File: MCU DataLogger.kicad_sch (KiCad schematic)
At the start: 0 parts

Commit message: Have added required symbols
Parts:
- added BT?: Battery, symbol Device:Battery
- added C? (x4): C, symbol Device:C
- added C? (x2): C_Polarized, symbol Device:C_Polarized
- added D? (x2): LED, symbol Device:LED
- added H? (x4): MountingHole, symbol Mechanical:MountingHole
- added R? (x7): R, symbol Device:R
- added U?: DS1337S+, SOIC127P600X175-8N, symbol DS1337S_:DS1337S+
- added U? (x2): 24LC1025, symbol Memory_EEPROM:24LC1025
- added U?: ATMEGA328P-AU, QFP80P900X900X120-32N, symbol ATMEGA328P-AU:ATMEGA328P-AU
- added Y? (x2): Crystal, symbol Device:Crystal
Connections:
- new net: U?.21 (GND), U?.3 (GND), U?.5 (GND)
- new net: U?.4 (VCC), U?.6 (VCC)
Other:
- added sheet Connectors (connectors.kicad_sch)

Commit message: Changes and add component values
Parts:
- removed C?: C_Polarized, symbol Device:C_Polarized
- C1, C4: renamed from C?; value C -> 0.1uF
- C2, C3: renamed from C?; value C -> 22pF
- C5: renamed from C?; value C_Polarized -> 100nF
- R1, R2: renamed from R?; value R -> 4.7K
- R3, R4, R6: renamed from R?; value R -> 10K
- R5, R7: renamed from R?; value R -> 330
- Y1: renamed from Y?; value Crystal -> 32.768 KHz
- Y2: renamed from Y?; value Crystal -> 16 MHz
- gave numbers to parts that had none: 11
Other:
- moved on the sheet: BT1, C1, C2, C3, C4, C5, D1, D2, R1, R2, R3, R4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

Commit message: Completed symbol-footprint associations.
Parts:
- BT1: footprint (none) -> Connector_PinHeader_2.54mm:PinHeader_1x02_P2.54mm_Vertical
- C1, C2, C3, C4, C5: footprint (none) -> Capacitor_SMD:C_0805_2012Metric
- D1, D2: footprint (none) -> LED_SMD:LED_0805_2012Metric
- H1, H2, H3, H4: footprint (none) -> MountingHole:MountingHole_2.1mm
- R1, R2, R3, R4, R5, R6, R7: footprint (none) -> Resistor_SMD:R_0805_2012Metric
- U1, U2: footprint (none) -> Package_SO:SOIC-8_5.23x5.23mm_P1.27mm
- U3: footprint SOIC127P600X175-8N -> Libraries:SOIC127P600X175-8N
- U4: footprint QFP80P900X900X120-32N -> Libraries:QFP80P900X900X120-32N
- Y1, Y2: footprint (none) -> Crystal:Crystal_SMD_5032-2Pin_5.0x3.2mm_HandSoldering

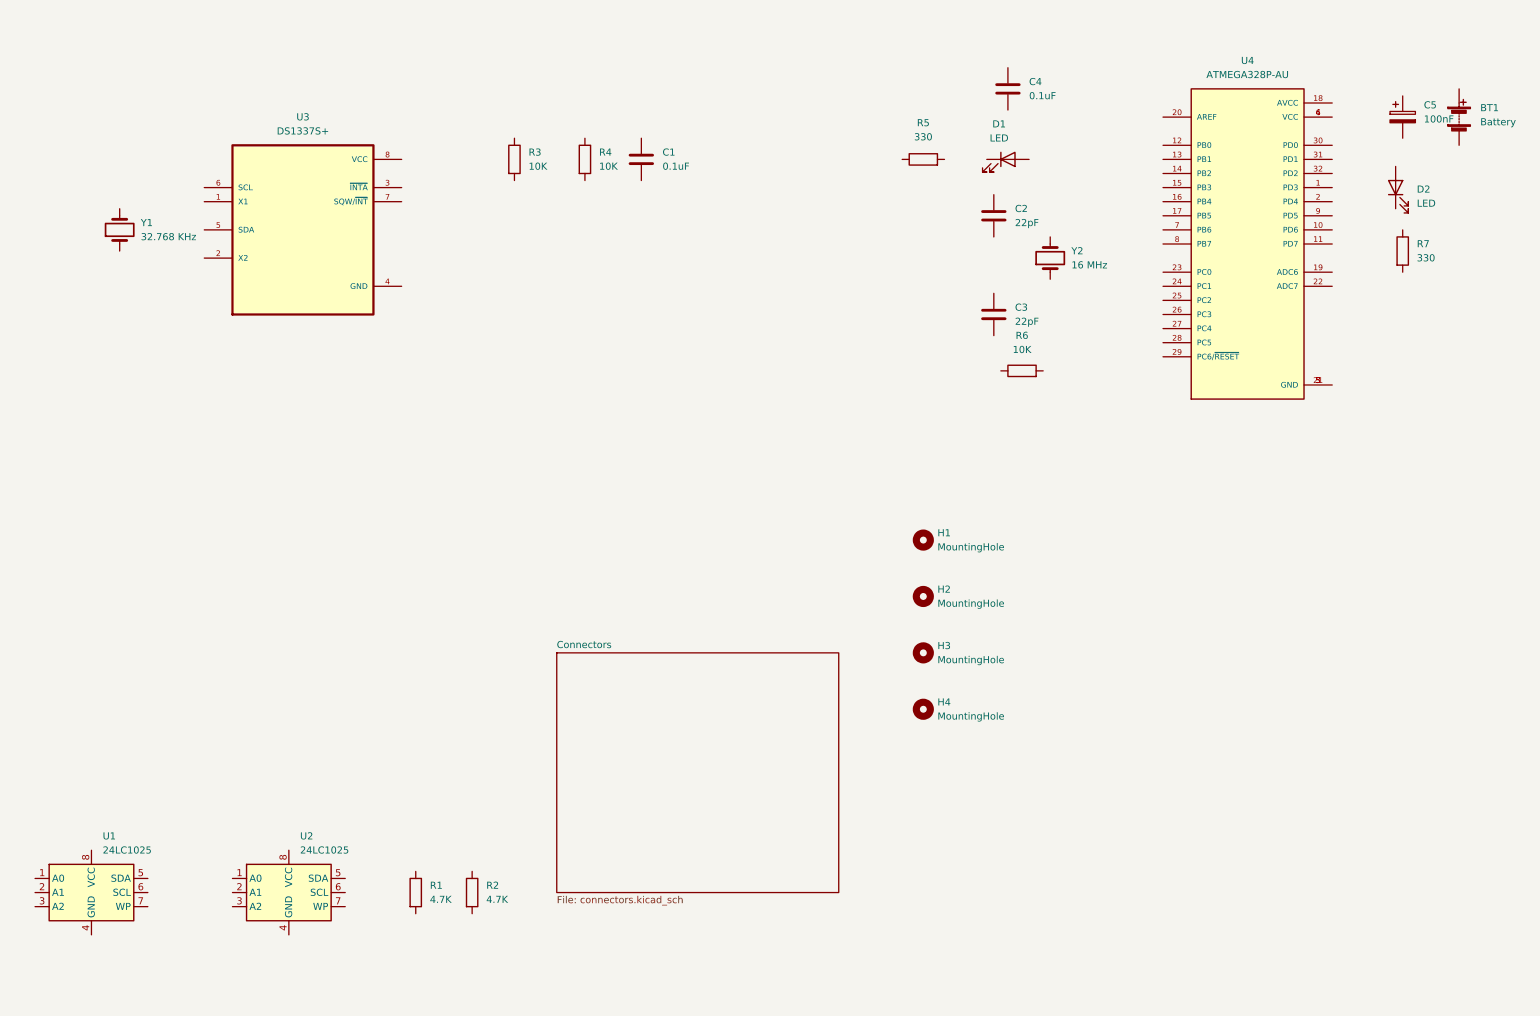
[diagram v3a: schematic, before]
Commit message: Completed wiring of main sheet.
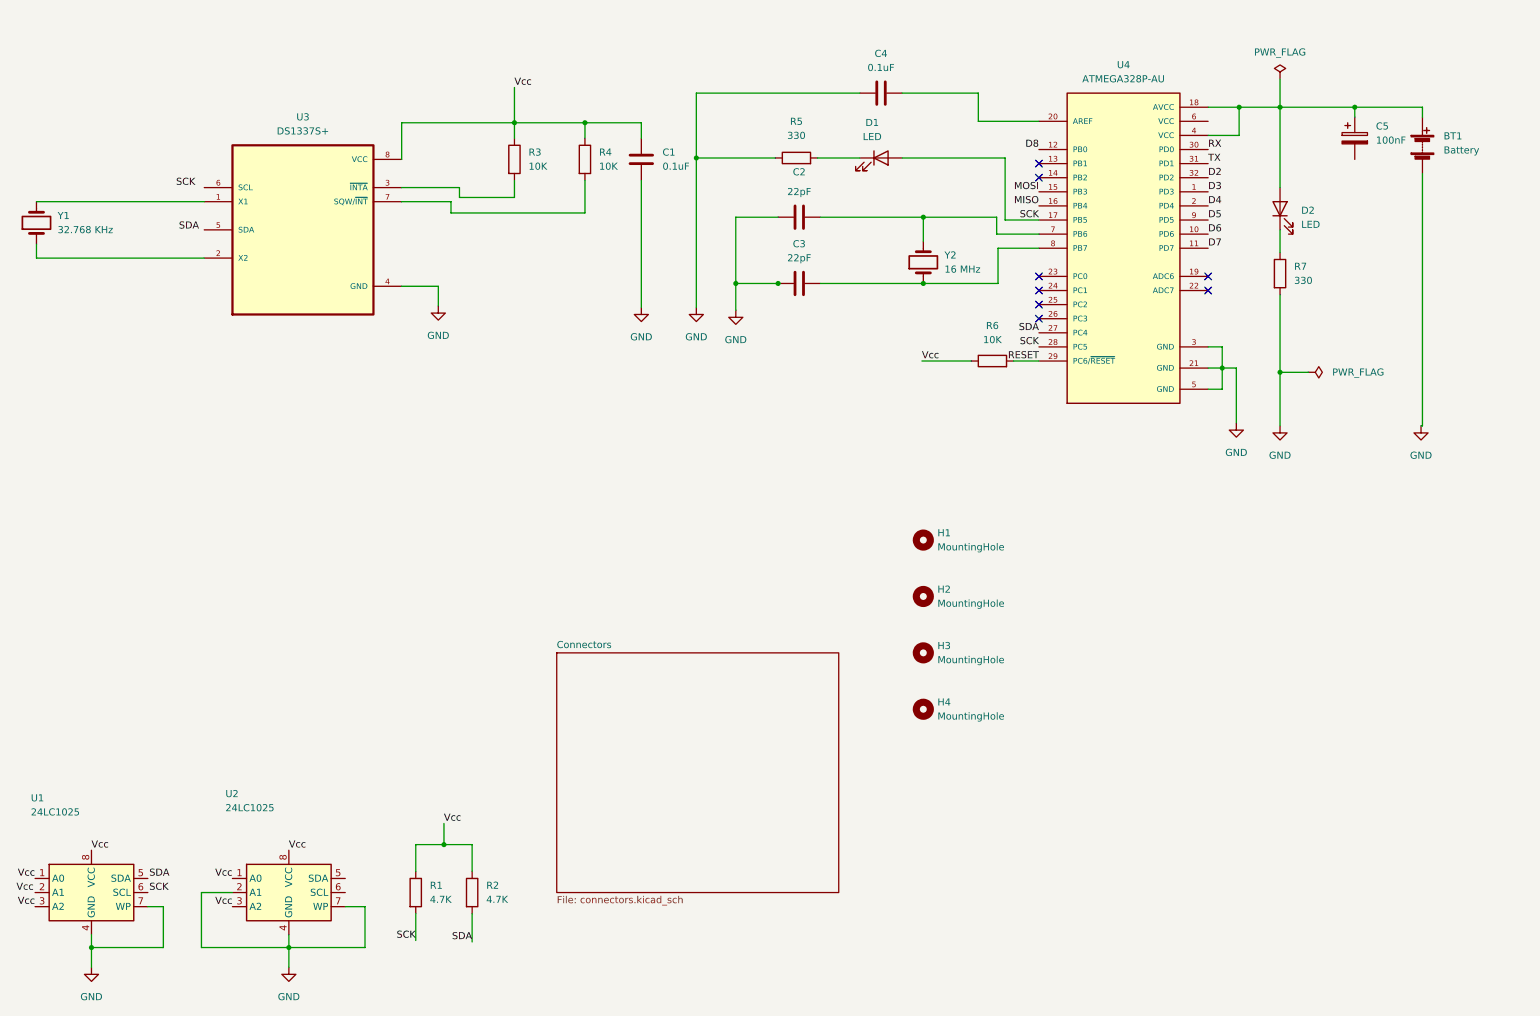
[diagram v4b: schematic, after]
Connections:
- net Vcc: now reaches R6.1
- net Vcc: now also R1.1, R2.1, U1.1 (A0), U1.3 (A2), U1.8 (VCC), U2.1 (A0), U2.3 (A2), U2.8 (VCC)
- net RESET: now reaches R6.2
- net RESET: now also U4.29 (PC6/~{RESET})
- net at U3.1 (X1): now also Y1.2
- net at U3.2 (X2): now also Y1.1
- net at U3.3 (~{INTA}): now also R3.2
- net GND: now reaches U3.4 (GND)
- net GND: now also BT1.2 (-), C1.2, C2.2, C3.1, C4.1, R5.1, R7.2, U1.4 (GND), U1.7 (WP), U2.2 (A1), U2.4 (GND), U2.7 (WP), U4.21 (GND), U4.3 (GND), U4.5 (GND)
- net at U3.7 (SQW/~{INT}): now also R4.2
- net at U3.8 (VCC): now also C1.1, R3.1, R4.1
- net at R7.1: now also D2.1 (K)
- net at C2.1: now also U4.7 (PB6), Y2.2
- net D3: now reaches U4.1 (PD3)
- net D6: now reaches U4.10 (PD6)
- net D7: now reaches U4.11 (PD7)
- net D8: now reaches U4.12 (PB0)
- net MOSI: now reaches U4.15 (PB3)
- net MISO: now reaches U4.16 (PB4)
- net SCK: now reaches U4.17 (PB5)
- net SCK: now also D1.2 (A), R1.2, U4.28 (PC5)
- net at U4.18 (AVCC): now also BT1.1 (+), C5.1, D2.2 (A), U4.4 (VCC)
- net D4: now reaches U4.2 (PD4)
- net at U4.20 (AREF): now also C4.2
- net SDA: now reaches U4.27 (PC4)
- net SDA: now also R2.2
- net RX: now reaches U4.30 (PD0)
- net TX: now reaches U4.31 (PD1)
- net D2: now reaches U4.32 (PD2)
- net at U4.6 (VCC): no longer U4.4 (VCC)
- net at U4.8 (PB7): now also C3.2, Y2.1
- net D5: now reaches U4.9 (PD5)
- net at R5.2: now also D1.1 (K)
- no-connect marks 0 -> 8
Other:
- moved on the sheet: BT1, C2, C3, C4, C5, D1, D2, R5, R6, R7, Y1, Y2

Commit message: Completed wiring
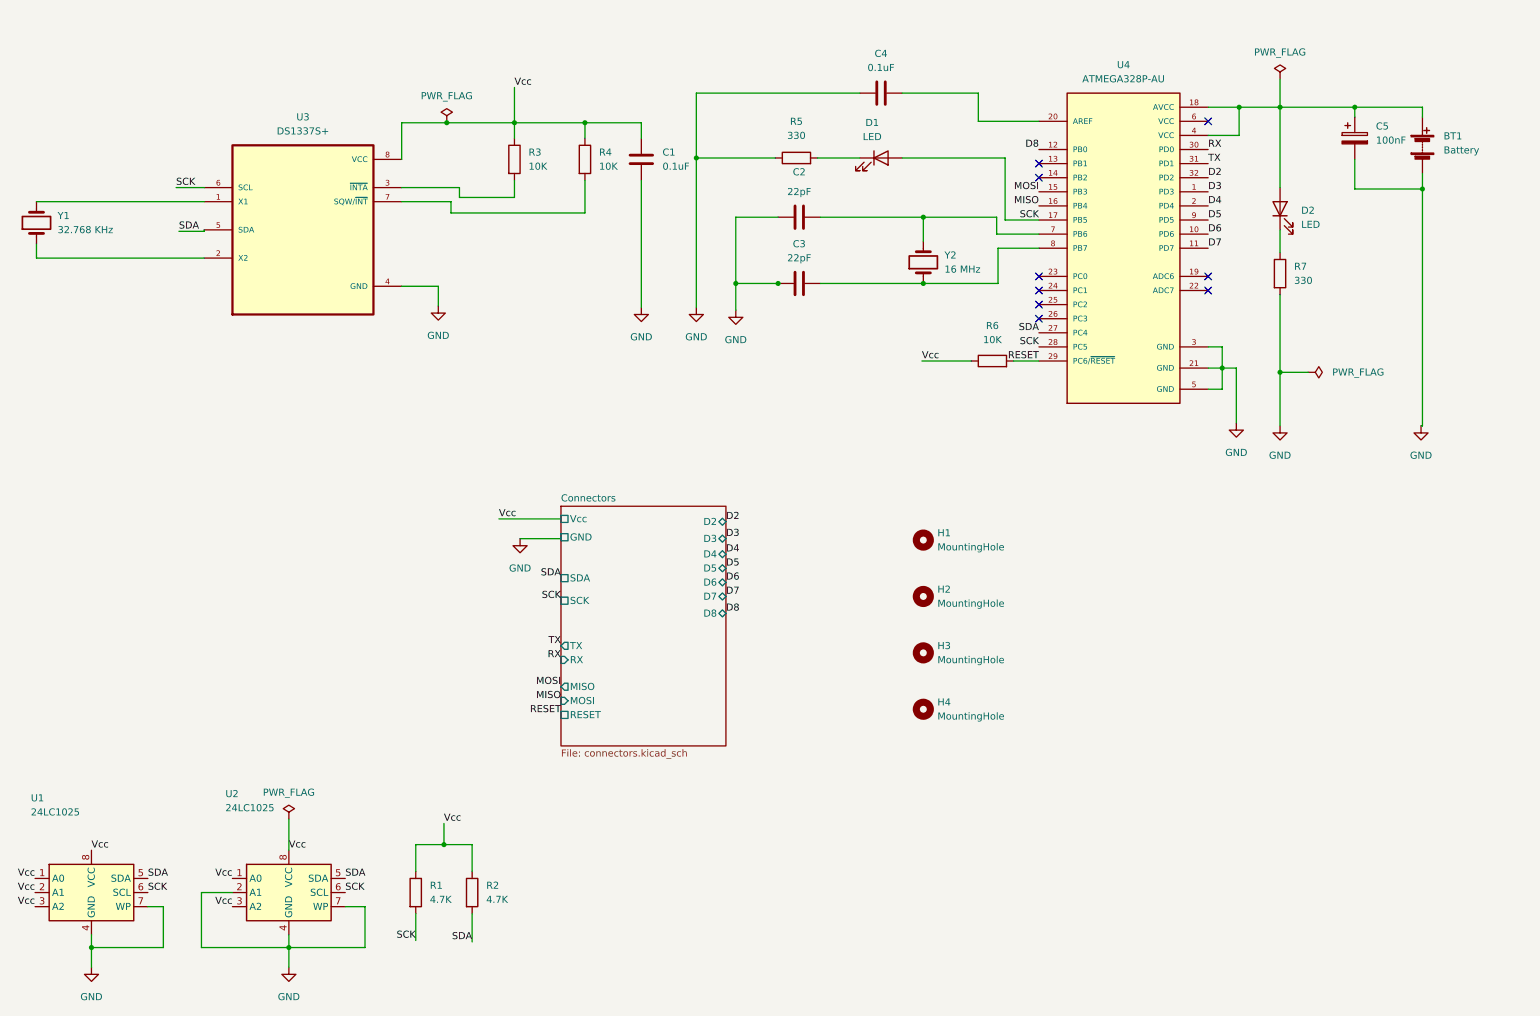
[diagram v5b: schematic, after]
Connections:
- net GND: now also C5.2
- net SCK: now also U1.6 (SCL), U2.6 (SCL), U3.6 (SCL)
- net SDA: now also U1.5 (SDA), U2.5 (SDA), U3.5 (SDA)
- net Vcc: now also U1.2 (A1)
- no-connect marks 8 -> 9
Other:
- sheet Connectors ports: added D2, D3, D4, D5, D6, D7, D8, GND, MISO, MOSI, RESET, RX, SCK, SDA, TX, Vcc; removed none
